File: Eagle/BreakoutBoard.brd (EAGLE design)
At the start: 77 x 25 mm, 13 parts

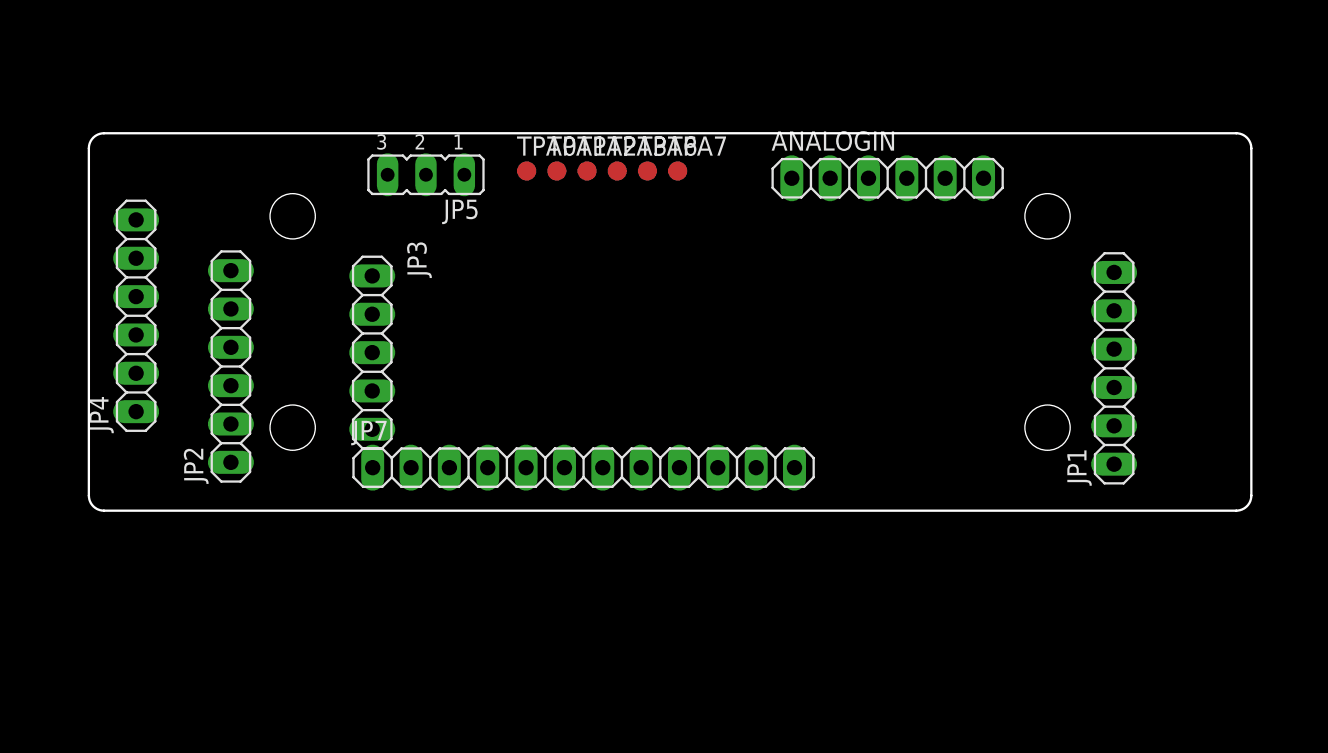
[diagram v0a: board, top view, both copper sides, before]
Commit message: Routed board
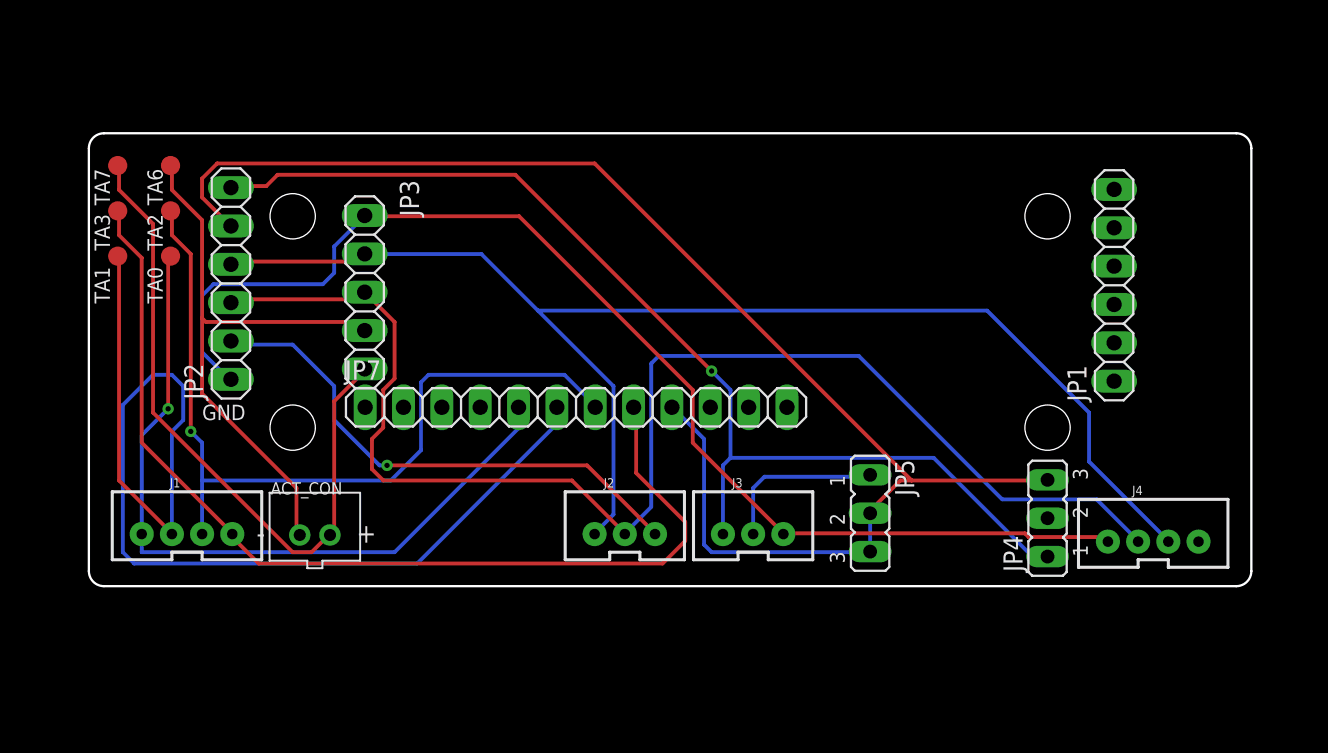
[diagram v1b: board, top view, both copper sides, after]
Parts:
- removed ANALOGIN: (no value), pinhead:1X06
- removed TPA0, TPA1, TPA2, TPA3, TPA6, TPA7: TPB1,27, testpad:B1,27
- added ACT_CON: (no value), adafruit:JST-PH-2-THM
- added J1: JOINTS_CON, SparkFun-Connectors:JST-4-PTH-VERT
- added J2: RPI_CTRL, SparkFun-Connectors:JST-3-PTH-VERT
- added J3: RPI_PWR, SparkFun-Connectors:JST-3-PTH-VERT
- added J4: I2C_CTRL, SparkFun-Connectors:JST-4-PTH-VERT
- added TA0, TA1, TA2, TA3, TA6, TA7: TPB1,27, testpad:B1,27
- JP3: value ARD_LEFTCOL -> ARD_LEFT
- JP4: value RPI_CONNECTOR -> PWR_SEL2; device pinhead:1X06 -> jumper:JP2
- JP5: value PWR_SELECT -> PWR_SEL
- JP7: value ARD_BOTTOMROW -> ARD_BOT
- moved JP4 61.8 mm to (63.5, -0.50)
- moved JP5 37.0 mm to (51.8, -0.17), turned to 270 degrees
- moved JP1 5.50 mm to (67.9, 14.9)
- moved JP2 5.50 mm to (9.41, 15.1)
- moved JP3 4.03 mm to (18.3, 14.5)
- moved JP7 4.03 mm to (32.3, 6.85)
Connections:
- new net GND2: JP7.11
- new net I2CPWR: J4.4
- new net N$4: JP4.2
- net 3V3: now also J3.1, JP4.1; no longer JP1.6, JP4.6
- net 5V: now also JP4.3; no longer JP1.5
- net A0: now also J1.1, TA0.TP; no longer ANALOGIN.1, TPA0.TP
- net A1: now also J1.2, TA1.TP; no longer ANALOGIN.2, TPA1.TP
- net A2: now also J1.3, TA2.TP; no longer ANALOGIN.3, TPA2.TP
- net A3: now also J1.4, TA3.TP; no longer ANALOGIN.4, TPA3.TP
- net A6: now also ACT_CON.2, TA6.TP; no longer ANALOGIN.5, TPA6.TP
- net A7: now also ACT_CON.1, TA7.TP; no longer ANALOGIN.6, TPA7.TP
- net GND: now also J3.3, J4.1; no longer JP1.1, JP4.1, JP7.11
- net OE: now also J2.3; no longer JP1.2, JP4.2
- net RPI5V: now also J3.2; no longer JP4.5
- net SCL: now also J2.2, J4.2; no longer JP1.3, JP4.3
- net SDA: now also J2.1, J4.3; no longer JP1.4, JP4.4
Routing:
- net 5V: track 0.00 -> 96.6 mm
- net SCL: track 0.00 -> 90.6 mm
- net SDA: track 0.00 -> 89.6 mm
- net GND: track 0.00 -> 80.7 mm
- net A1: track 0.00 -> 78.9 mm
- net 3V3: track 0.00 -> 72.8 mm, vias 0 -> 1
- net A3: track 0.00 -> 66.4 mm
- net A2: track 0.00 -> 54.8 mm, vias 0 -> 1
- net A0: track 0.00 -> 50.2 mm, vias 0 -> 1
- net A7: track 0.00 -> 45.3 mm
- net A6: track 0.00 -> 39.2 mm
- net OE: track 0.00 -> 34.8 mm, vias 0 -> 1
- net RPI5V: track 0.00 -> 11.2 mm
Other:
- board size 77 x 25 mm -> 77 x 30 mm
- board text added: "GND"

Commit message: Added breakout board Added servo bracket renderings and dimensions
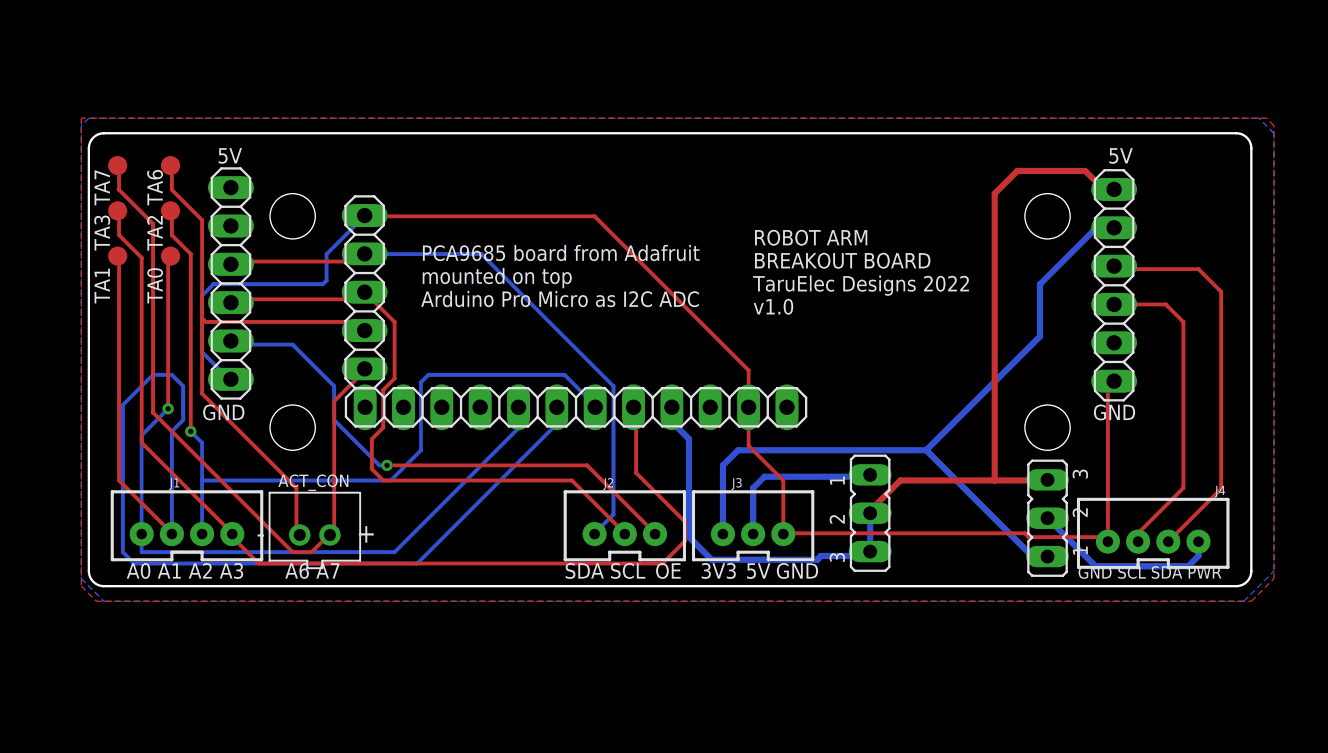
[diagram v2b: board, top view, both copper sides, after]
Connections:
- removed net GND2: JP7.11
- removed net N$4: JP4.2
- net 3V3: now also JP1.5, JP2.5; no longer JP2.6
- net 5V: now also JP1.6, JP2.6; no longer JP2.5
- net GND: now also JP1.1, JP7.11
- net I2CPWR: now also JP4.2
- net OE: now also JP1.2
- net SCL: now also JP1.3
- net SDA: now also JP1.4
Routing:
- net 5V: track 96.6 -> 65.3 mm
- net SCL: track 90.6 -> 62.0 mm
- net SDA: track 89.6 -> 65.9 mm
- net 3V3: track 72.8 -> 50.0 mm, vias 1 -> 0
- net GND: track 80.7 -> 94.5 mm
- net I2CPWR: track 0.00 -> 12.6 mm
- added copper zone on layer 1, net GND
- added copper zone on layer 16, net GND
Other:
- board text added: "3V3"
- board text added: "5V"
- board text added: "A0 A1 A2 A3"
- board text added: "A6 A7"
- board text added: "GND SCL SDA PWR"
- board text added: "OE"
- board text added: "PCA9685 board from Adafruit mounted on top Arduino Pro Micro as I2C ADC"
- board text added: "ROBOT ARM BREAKOUT BOARD TaruElec Designs 2022 v1.0"
- board text added: "SCL"
- board text added: "SDA"

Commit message: Done some refactoring and readjusting
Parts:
- removed ACT_CON: (no value), adafruit:JST-PH-2-THM
- removed J1: JOINTS_CON, SparkFun-Connectors:JST-4-PTH-VERT
- removed J2: RPI_CTRL, SparkFun-Connectors:JST-3-PTH-VERT
- removed J3: RPI_PWR, SparkFun-Connectors:JST-3-PTH-VERT
- removed J4: I2C_CTRL, SparkFun-Connectors:JST-4-PTH-VERT
- removed TA0, TA1, TA2, TA3, TA6, TA7: TPB1,27, testpad:B1,27
- added J5: RPIDATA, Connector:B3B-XH-A
- added J6: RPIPWR, Connector:B3B-XH-A
- added J7: I2C, Connector:B4B-XH-A
- added J8: JOINTS1234, Connector:B4B-XH-A
- added J9: JOINTS56, Connector:B2B-XH-A
- added JP10: SDA, Connector:1X01
- added JP11, JP21, JP30, JP34: GND, Connector:1X01
- added JP12: D10, Connector:1X01
- added JP13: D11, Connector:1X01
- added JP14: D12, Connector:1X01
- added JP15: D13, Connector:1X01
- added JP16: A0, Connector:1X01
- added JP17: A1, Connector:1X01
- added JP18: A2, Connector:1X01
- added JP19: A3, Connector:1X01
- added JP20: 5V, Connector:1X01
- added JP22: RAW, Connector:1X01
- added JP23: D8, Connector:1X01
- added JP24: D7, Connector:1X01
- added JP25: D6, Connector:1X01
- added JP26: D5, Connector:1X01
- added JP27: D4, Connector:1X01
- added JP28: D3, Connector:1X01
- added JP29: D2, Connector:1X01
- added JP31: RST, Connector:1X01
- added JP32: TRXI, Connector:1X01
- added JP33, JP37: TX0, Connector:1X01
- added JP35: A_VCC, Connector:1X01
- added JP36: RXI, Connector:1X01
- added JP38: DTR, Connector:1X01
- added JP6: A7, Connector:1X01
- added JP8: A6, Connector:1X01
- added JP9: SCL, Connector:1X01
- JP3: value ARD_LEFT -> D9; device pinhead:1X05 -> Connector:1X01
- JP7: value ARD_BOT -> RST; device pinhead:1X12 -> Connector:1X01
- moved JP5 20.2 mm to (33.0, -7.62)
- moved JP7 15.2 mm to (39.4, 20.3)
- moved JP4 8.75 mm to (68.6, -7.62)
- moved JP3 6.11 mm to (16.5, 20.3), turned to 0 degrees
- moved JP2 2.95 mm to (10.2, 12.2)
- moved JP1 2.77 mm to (68.3, 12.2)
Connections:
- new net DTR: JP38.1
- new net RXI: JP36.1
- new net TX0: JP37.1
- net 3V3: now also J6.3; no longer J3.1
- net 5V: now also JP20.1, JP35.1; no longer JP7.9
- net A0: now also J8.1, JP16.1; no longer J1.1, JP7.5, TA0.TP
- net A1: now also J8.2, JP17.1; no longer J1.2, JP7.6, TA1.TP
- net A2: now also J8.3, JP18.1; no longer J1.3, JP7.7, TA2.TP
- net A3: now also J8.4, JP19.1; no longer J1.4, JP7.8, TA3.TP
- net A6: now also J9.2, JP8.1; no longer ACT_CON.2, JP3.4, TA6.TP
- net A7: now also J9.1, JP6.1; no longer ACT_CON.1, JP3.5, TA7.TP
- net D10: now also JP12.1; no longer JP7.1
- net D11: now also JP13.1; no longer JP7.2
- net D12: now also JP14.1; no longer JP7.3
- net D13: now also JP15.1; no longer JP7.4
- net GND: now also J6.1, J7.4, JP11.1, JP21.1, JP30.1, JP34.1; no longer J3.3, J4.1, JP3.1, JP7.11
- net I2CPWR: now also J7.1; no longer J4.4
- net OE: now also J5.1; no longer J2.3
- net RAW: now also JP22.1; no longer JP7.12
- net RPI5V: now also J6.2; no longer J3.2
- net RST: now also JP7.1; no longer JP7.10
- net SCL: now also J5.2, J7.3, JP9.1; no longer J2.2, J4.2, JP3.3
- net SDA: now also J5.3, J7.2, JP10.1; no longer J2.1, J4.3, JP3.2
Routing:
- net GND: track 94.5 -> 0.00 mm
- net A1: track 78.9 -> 0.00 mm
- net A3: track 66.4 -> 0.00 mm
- net SDA: track 65.9 -> 0.00 mm
- net 5V: track 65.3 -> 0.00 mm
- net SCL: track 62.0 -> 0.00 mm
- net A2: track 54.8 -> 0.00 mm, vias 1 -> 0
- net A0: track 50.2 -> 0.00 mm, vias 1 -> 0
- net 3V3: track 50.0 -> 0.00 mm
- net A7: track 45.3 -> 0.00 mm
- net A6: track 39.2 -> 0.00 mm
- net OE: track 34.8 -> 0.00 mm, vias 1 -> 0
- net I2CPWR: track 12.6 -> 0.00 mm
- net RPI5V: track 11.2 -> 0.00 mm
- removed copper zone on layer 1, net GND
- removed copper zone on layer 16, net GND
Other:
- board size 77 x 30 mm -> 83.8 x 45.7 mm
- board text added: "NC"
- board text added: "Place Arduino Here"
- board text added: "RPI5V"
- board text added: "VCC"
- board text removed: "A0 A1 A2 A3"
- board text removed: "A6 A7"
- board text removed: "GND SCL SDA PWR"
- board text removed: "PCA9685 board from Adafruit mounted on top Arduino Pro Micro as I2C ADC"
- board text removed: "ROBOT ARM BREAKOUT BOARD TaruElec Designs 2022 v1.0"
